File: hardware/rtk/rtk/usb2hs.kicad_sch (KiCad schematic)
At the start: 5 parts, among them U8 USB3300-EZK

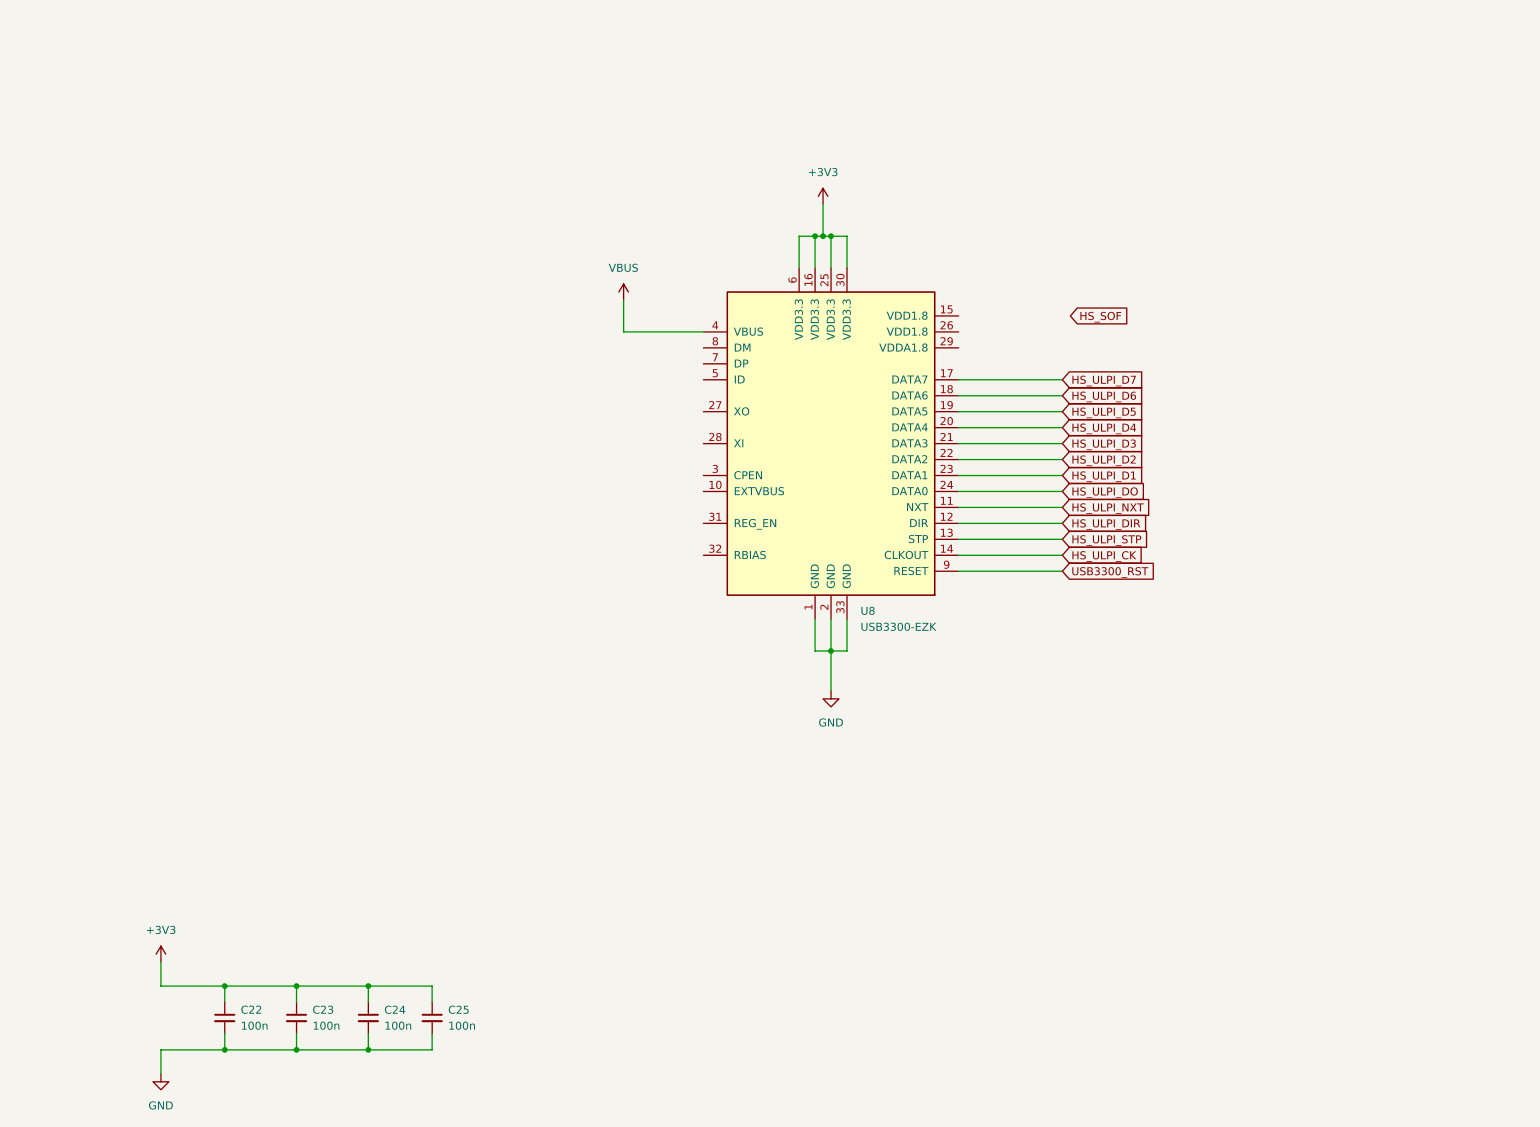
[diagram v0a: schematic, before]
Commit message: Schematic progress: all sheets ~90% complete (#182)
- power.kicad_sch: PSU, BQ24075, LiPo connector, USB-C power path
- stm32f765vit.kicad_sch: F765VIT pin assignments, SPI2/I2C4/SDMMC1/UART7/8/USART3
- usb2hs.kicad_sch: USB3300 ULPI, 24MHz TCXO (ASTX-H11-24MHz), USB-C connector, diff pair nets USB_D+/USB_D-
- zed-f9p-05b.kicad_sch: ZED-F9P-05B connections
- rtk-base.ioc: DIO1 corrected to GPIO_Input, LSM6DSOX CS removed (I2C mode, CS tied high in schematic), DIO2 label typo fixed
- rtk.kicad_pcb/pro: project settings updated

Co-Authored-By: Claude Sonnet 4.6 <noreply@anthropic.com>
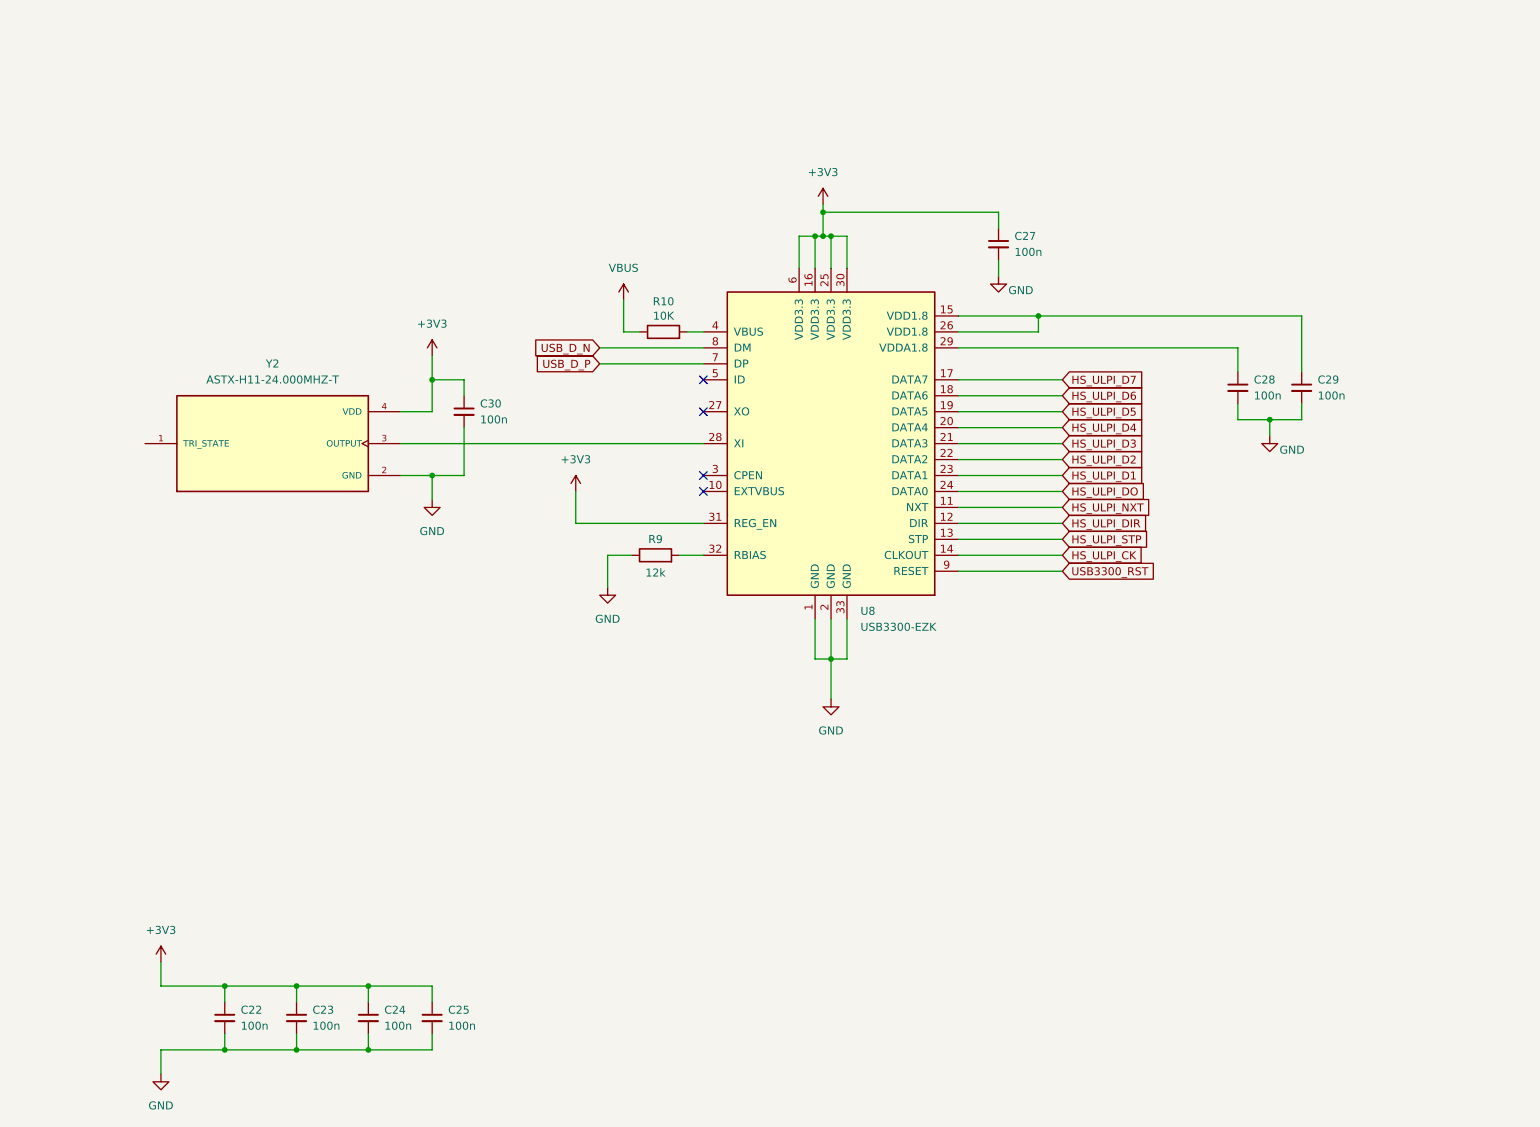
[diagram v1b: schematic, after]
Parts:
- added C27, C28, C29, C30: 100n, Capacitor_SMD:C_0805_2012Metric_Pad1.18x1.45mm_HandSolder, symbol Device:C_Small
- added R10: 10K, Resistor_SMD:R_0805_2012Metric_Pad1.20x1.40mm_HandSolder, symbol Device:R
- added R9: 12k, Resistor_SMD:R_0805_2012Metric_Pad1.20x1.40mm_HandSolder, symbol Device:R
- added Y2: ASTX-H11-24.000MHZ-T, ASTX-H11-16.000MHZ-T:XTAL_ASTX-H11-16.000MHZ-T, symbol ASTX-H11-16.000MHZ-T:ASTX-H11-16.000MHZ-T
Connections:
- net +3V3: now also U8.31 (REG_EN), C27.1, C30.1, Y2.4 (VDD)
- net GND: now also C27.2, C28.2, C29.2, C30.2, R9.1, Y2.2 (GND)
- net VBUS: now also R10.1; no longer U8.4 (VBUS)
- net at U8.15 (VDD1.8): now also U8.26 (VDD1.8), C29.1
- net at U8.28 (XI): now also Y2.3 (OUTPUT)
- net at U8.29 (VDDA1.8): now also C28.1
- net at U8.32 (RBIAS): now also R9.2
- net USB_D_P: now reaches U8.7 (DP)
- net USB_D_N: now reaches U8.8 (DM)
- new net: R10.2, U8.4 (VBUS)
- no-connect marks 0 -> 4

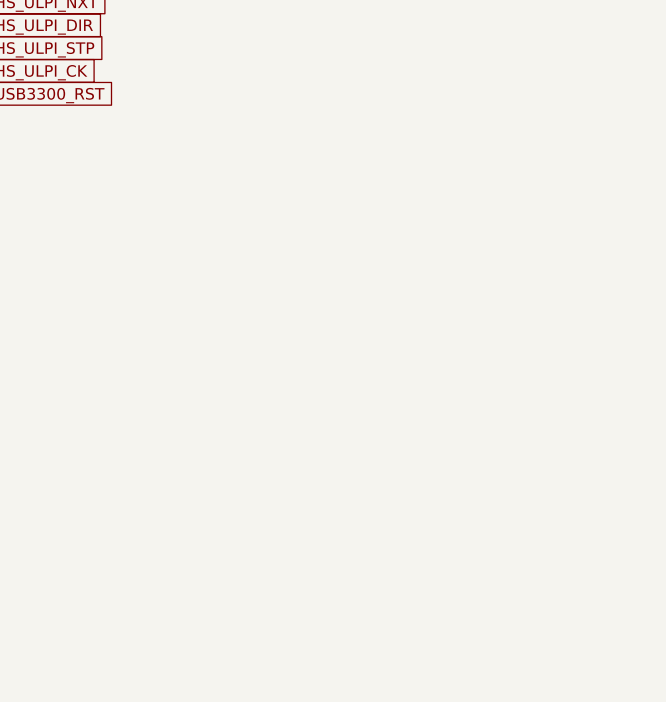
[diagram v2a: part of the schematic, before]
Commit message: STM32F765VIT sheet review fixes (#182)
- VBAT tied to +3V3 (not raw LiPo)
- CORE1262 RXEN/TXEN reassigned to PC6/PC7 GPIO outputs (init low)
- I2C4 external 4k7 pull-ups added on SCL/SDA
- BOOT0 pull-down + test point added
- LSM6DSOX CS tied to +3V3, SDO/SA0 tied to GND (addr 0x6A)
- ESP32-S3-ZERO: 5V NC, powered via 3V3 rail; GP1-GP5 wired to PE2-PE6
- nPGOOD/nCHG/SYSOFF added to STM32 sheet
- MMC5603NJ sub-board connector added (I2C4, 2x GPIO, 3V3, GND)
- rtk-base.ioc: PC6/PC7 RXEN/TXEN, PE2-PE6 spare, PD7/PD10/PD11

Co-Authored-By: Claude Sonnet 4.6 <noreply@anthropic.com>
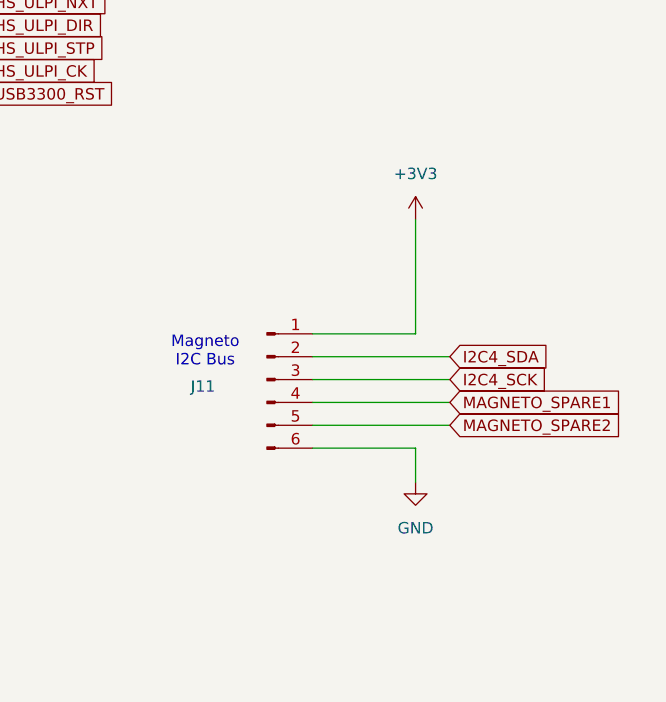
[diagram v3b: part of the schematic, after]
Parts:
- added J11: Conn_01x06_Pin, Connector_PinHeader_2.54mm:PinHeader_1x06_P2.54mm_Vertical, symbol Connector:Conn_01x06_Pin
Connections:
- net +3V3: now also J11.1 (Pin_1)
- net GND: now also J11.6 (Pin_6)
- new net I2C4_SCK: J11.3 (Pin_3)
- new net I2C4_SDA: J11.2 (Pin_2)
- new net MAGNETO_SPARE1: J11.4 (Pin_4)
- new net MAGNETO_SPARE2: J11.5 (Pin_5)
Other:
- note added: "Magneto I2C Bus"

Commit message: USB2HS sheet review fixes; ZED-F9P and misc updates (#182)
- usb2hs.kicad_sch: CPEN tied to GND, VDD1.8 caps changed to 470nF,
  PRTR5V0U2X ESD TVS added on USB_D+/D-, MMC5603NJ connector added
- stm32f765vit.kicad_sch: ESP32 GP1-GP5 wired to PE2-PE6
- docs/reference/psu/README.md: PRTR5V0U2X ESD TVS entry added

Co-Authored-By: Claude Sonnet 4.6 <noreply@anthropic.com>
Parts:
- added D2, D3: PRTR5V0U2X, Package_TO_SOT_SMD:SOT-143, symbol Power_Protection:PRTR5V0U2X
- C28, C29: value 100n -> 470n
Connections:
- net +3V3: now also D2.4 (VCC), D3.4 (VCC)
- net GND: now also U8.3 (CPEN), D2.1 (GND), D3.1 (GND)
- net USB_D_N: now also D3.3 (I/O2)
- net USB_D_P: now also D2.3 (I/O2)
- new net USB_D2_N: D3.2 (I/O1)
- new net USB_D2_P: D2.2 (I/O1)
- no-connect marks 4 -> 3
